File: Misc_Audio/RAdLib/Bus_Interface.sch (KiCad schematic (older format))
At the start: 18 parts, among them J1 Raspberry_Pi_2_3, J2 UART_Header, J3 Power_Output_Header, J4 I2C_Header, Q201 2N7000, U201 74LVC245A, U202 74HCT245, U203 74AHCT125, U204 M24C01-FDW

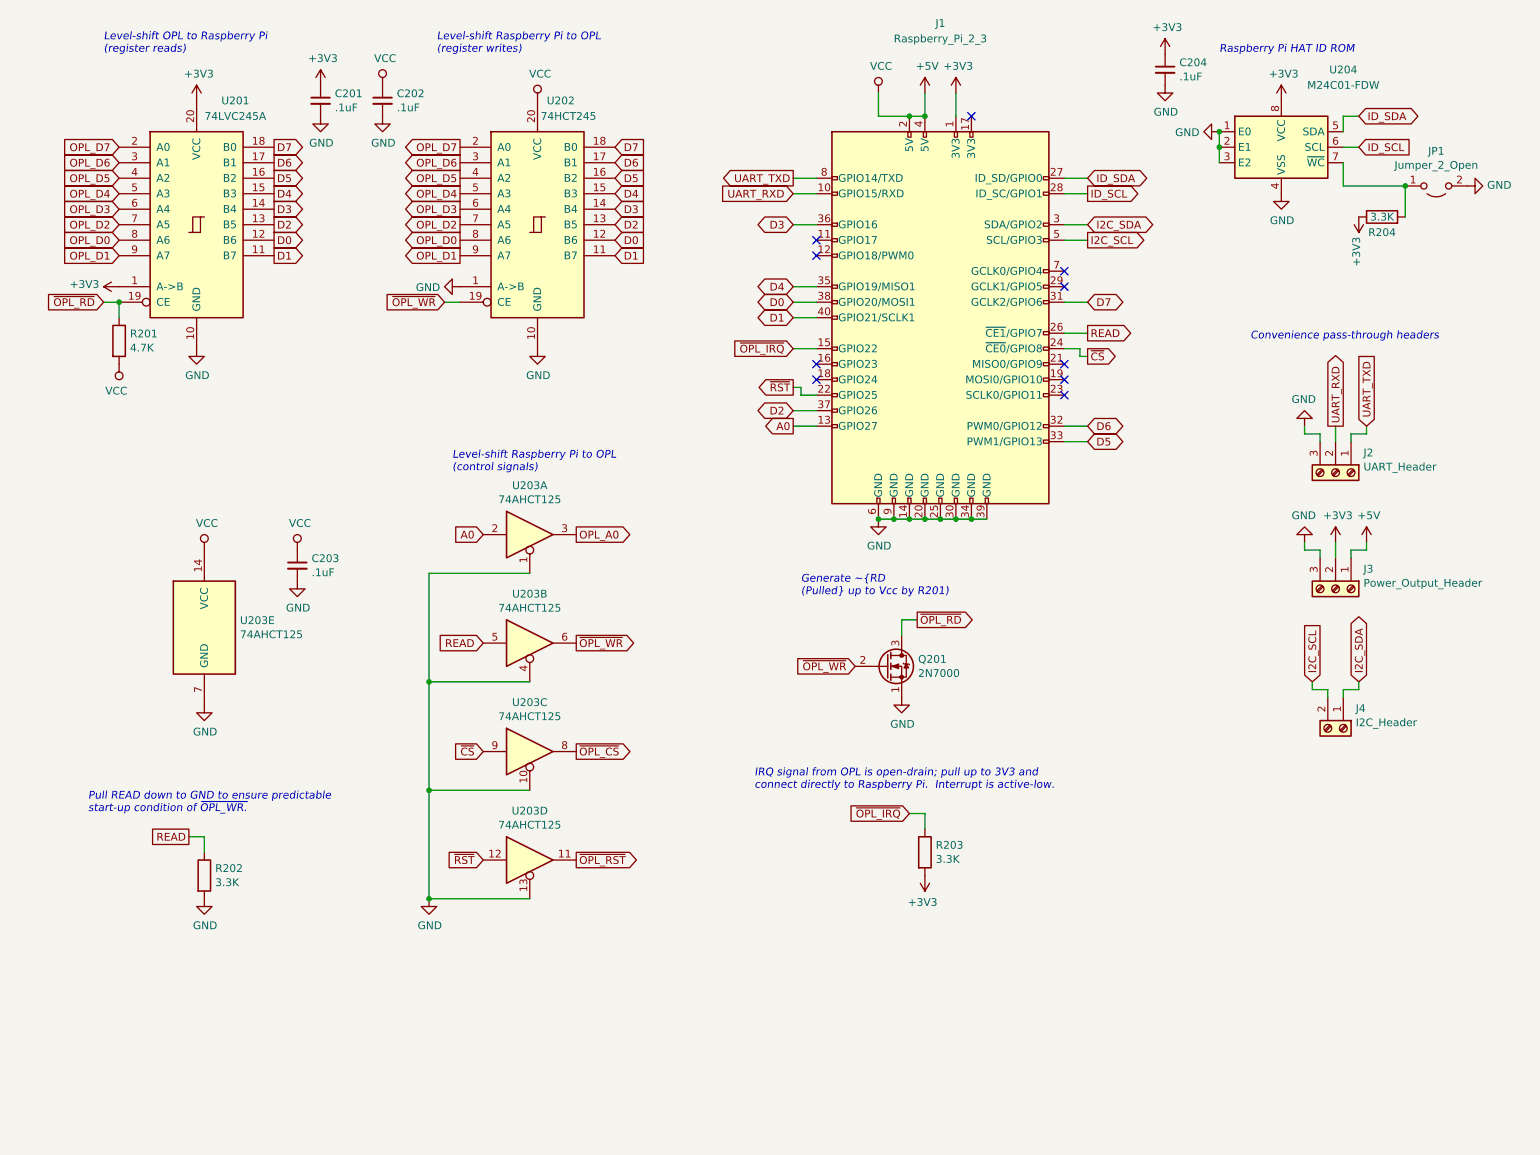
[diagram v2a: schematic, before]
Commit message: Initial rework to simplify the bus interface (removing U202 and U203).
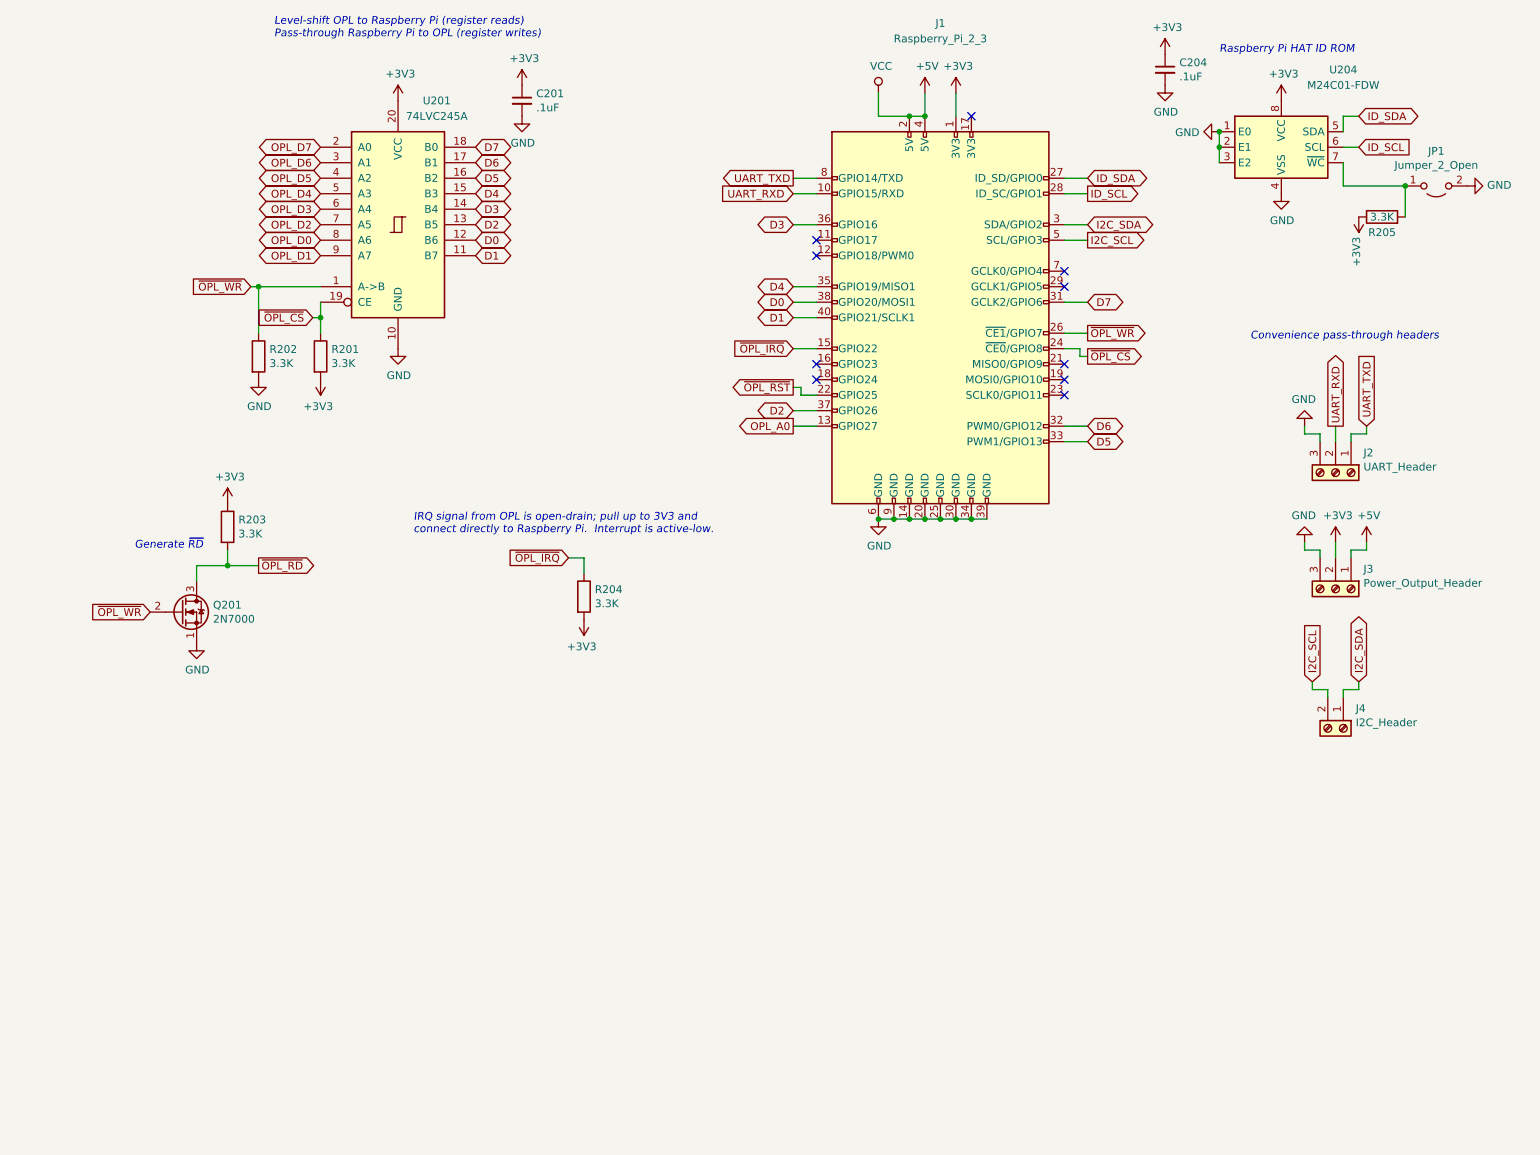
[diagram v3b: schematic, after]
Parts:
- removed C202, C203: .1uF, Capacitor_THT:C_Disc_D5.0mm_W2.5mm_P2.50mm, symbol Device:C_Small
- removed U202: 74HCT245, Package_DIP:DIP-20_W7.62mm, symbol 74xx:74HC245
- removed U203: 74AHCT125, Package_DIP:DIP-14_W7.62mm, symbol 74xx:74LS125
- added R203: 3.3K, Resistor_THT:R_Axial_DIN0204_L3.6mm_D1.6mm_P5.08mm_Horizontal, symbol Device:R
- R201: value 4.7K -> 3.3K; Part Xicon 270-4.7K/REEL-RC -> Xicon 270-3.3K/REEL-RC
- renumbered R203 to R204, R204 to R205
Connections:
- net A0 is gone; now on net OPL_A0: J1.13 (GPIO27)
- net READ is gone; now on net ~OPL_WR: J1.26 (~CE1~/GPIO7), R202.1
- net ~CS is gone; now on net ~OPL_CS: J1.24 (~CE0~/GPIO8)
- net ~RST is gone; now on net ~OPL_RST: J1.22 (GPIO25)
- net +3V3: now also R201.2, R203.1; no longer U201.1 (A->B)
- net +5V: no longer R201.2
- net ~OPL_CS: now also R201.1, U201.19 (CE)
- net ~OPL_RD: now also R203.2; no longer R201.1, U201.19 (CE)
- net ~OPL_WR: now also U201.1 (A->B)
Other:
- note added: "Generate ~RD"
- note added: "Level-shift OPL to Raspberry Pi (register reads)\nPass-through Raspberry Pi to OPL (register writes)"
- note removed: "Generate ~RD\n(Pulled up to Vcc by R201)"
- note removed: "Level-shift OPL to Raspberry Pi\n(register reads)"
- note removed: "Level-shift Raspberry Pi to OPL\n(control signals)"
- note removed: "Level-shift Raspberry Pi to OPL\n(register writes)"
- note removed: "Pull READ down to GND to ensure predictable\nstart-up condition of ~OPL_WR."
- moved on the sheet: C201, Q201, R201, R202, R204, U201

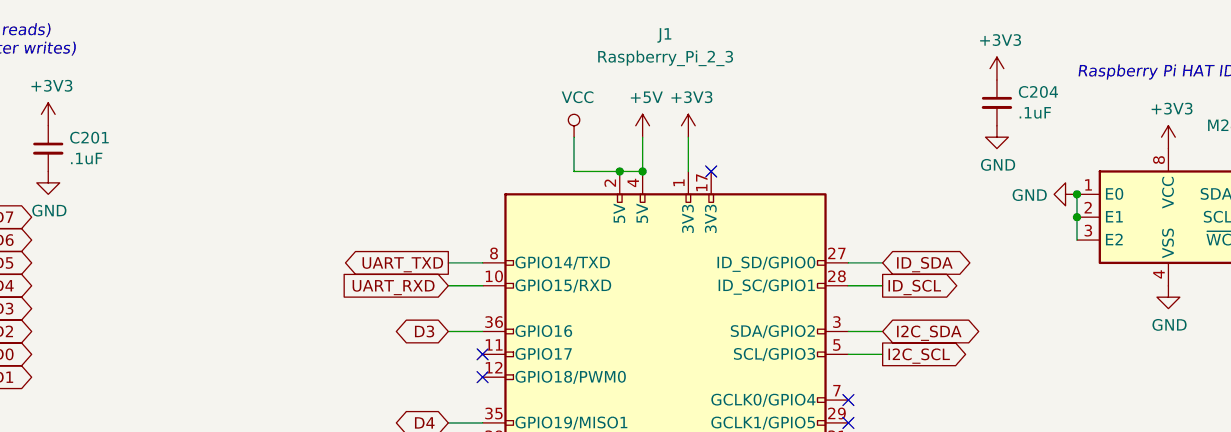
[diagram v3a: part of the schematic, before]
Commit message: Rework the audio output section as an AC-coupled emitter-follower.
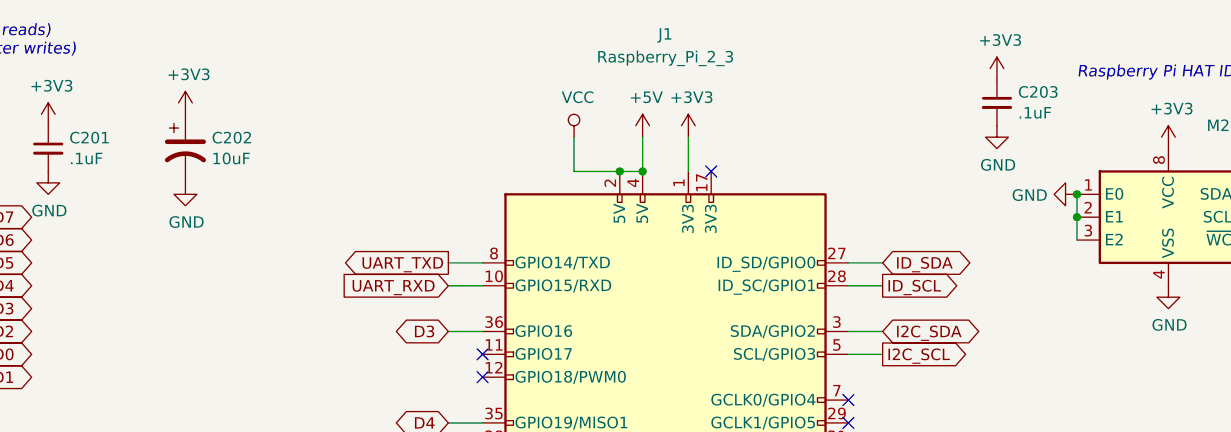
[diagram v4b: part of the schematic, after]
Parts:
- added C202: 10uF, Capacitor_THT:CP_Radial_D5.0mm_P2.50mm, symbol Device:CP1
- renumbered C204 to C203
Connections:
- net +3V3: now also C202.1
- net GND: now also C202.2
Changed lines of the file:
@@
 $EndComp
 $Comp
-L Device:C_Small C204
+L Device:C_Small C203
 U 1 1 5DA66B96
 P 7800 1050
-F 0 "C204" H 7892 1096 50  0000 L CNN
+F 0 "C203" H 7892 1096 50  0000 L CNN
 F 1 ".1uF" H 7892 1005 50  0000 L CNN
 F 2 "Capacitor_THT:C_Disc_D5.0mm_W2.5mm_P2.50mm" H 7800 1050 50  0001 C CNN
@@
 Wire Wire Line
 	1750 4150 1750 4250
+$Comp
+L Device:CP1 C202
+U 1 1 5DD1333D
+P 4250 1250
+F 0 "C202" H 4365 1296 50  0000 L CNN
+F 1 "10uF" H 4365 1205 50  0000 L CNN
+F 2 "Capacitor_THT:CP_Radial_D5.0mm_P2.50mm" H 4250 1250 50  0001 C CNN
+F 3 "~" H 4250 1250 50  0001 C CNN
+	1    4250 1250
+	1    0    0    -1
+$EndComp
+$Comp
+L power:GND #PWR0133
+U 1 1 5DD13EBB
+P 4250 1400
+F 0 "#PWR0133" H 4250 1150 50  0001 C CNN
+F 1 "GND" H 4255 1227 50  0000 C CNN
+F 2 "" H 4250 1400 50  0001 C CNN
+F 3 "" H 4250 1400 50  0001 C CNN
+	1    4250 1400
+	1    0    0    -1
+$EndComp
+$Comp
+L power:+3V3 #PWR0134
+U 1 1 5DD145BD
+P 4250 1100
+F 0 "#PWR0134" H 4250 950 50  0001 C CNN
+F 1 "+3V3" H 4265 1273 50  0000 C CNN
+F 2 "" H 4250 1100 50  0001 C CNN
+F 3 "" H 4250 1100 50  0001 C CNN
+	1    4250 1100
+	1    0    0    -1
+$EndComp
 $EndSCHEMATC

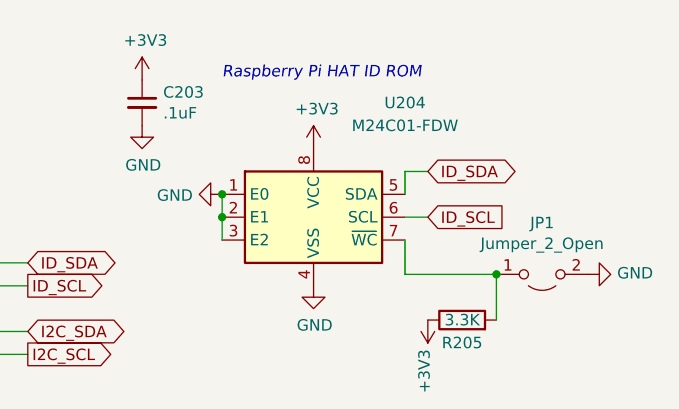
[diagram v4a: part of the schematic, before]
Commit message: Use a more generic part # for the ID ROM.
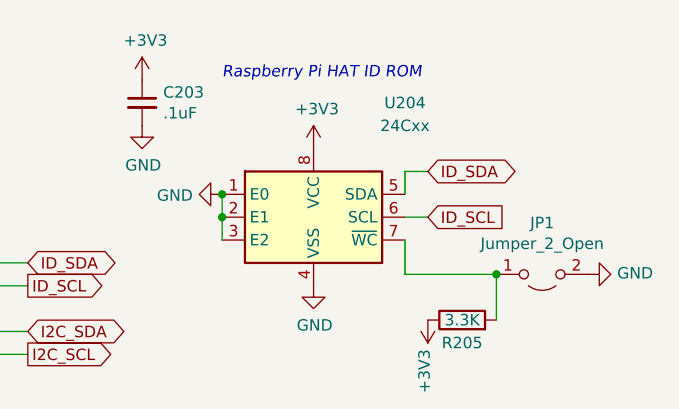
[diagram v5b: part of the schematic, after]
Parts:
- U204: value M24C01-FDW -> 24Cxx
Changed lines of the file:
@@
 P 8550 1550
 F 0 "U204" H 8950 2050 50  0000 C CNN
-F 1 "M24C01-FDW" H 8950 1950 50  0000 C CNN
+F 1 "24Cxx" H 8950 1950 50  0000 C CNN
 F 2 "Package_DIP:DIP-8_W7.62mm_Socket" H 8550 1900 50  0001 C CNN
 F 3 "http://www.st.com/content/ccc/resource/technical/document/datasheet/b0/d8/50/40/5a/85/49/6f/DM00071904.pdf/files/DM00071904.pdf/jcr:content/translations/en.DM00071904.pdf" H 8600 1050 50  0001 C CNN
